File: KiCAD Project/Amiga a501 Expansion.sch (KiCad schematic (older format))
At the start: 4 parts, among them J1 Conn_02x28_Odd_Even, U1 AS7C4098A, U2 AS7C4098A

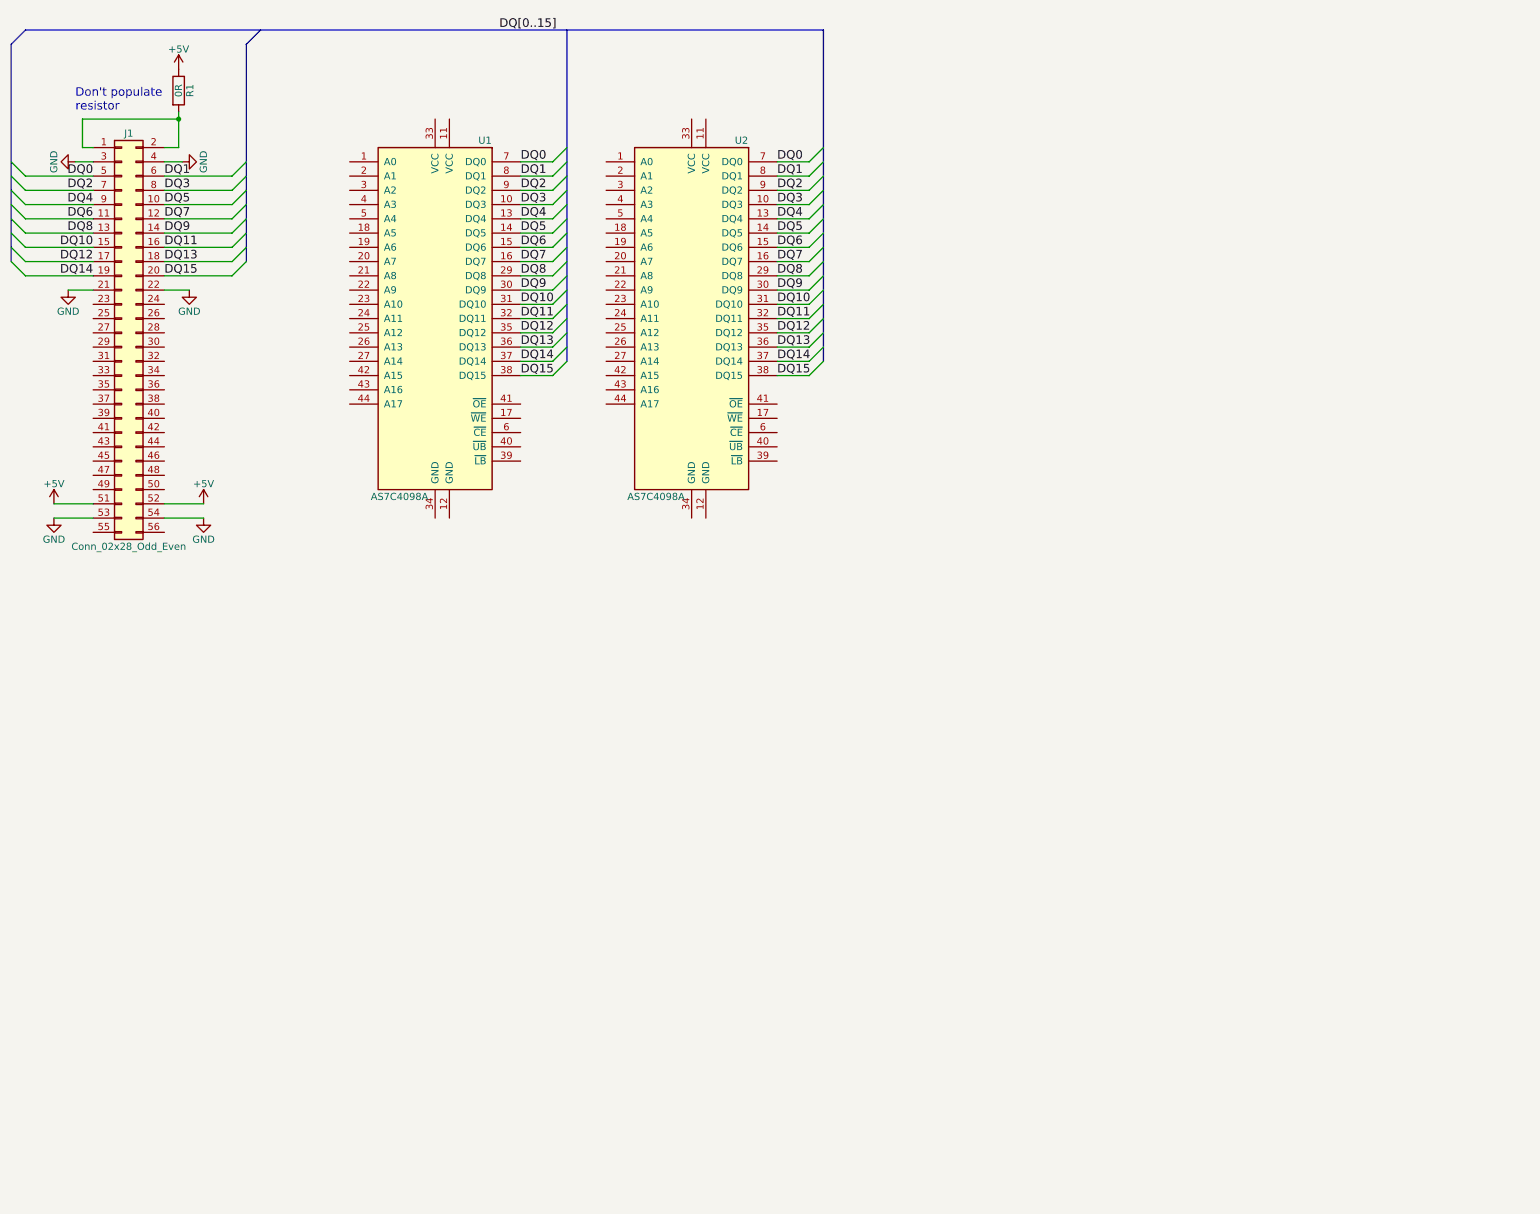
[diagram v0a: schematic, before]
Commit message: Work on verilog files. Started ram controller, made a flip flop array. Learning verilator synthesis now
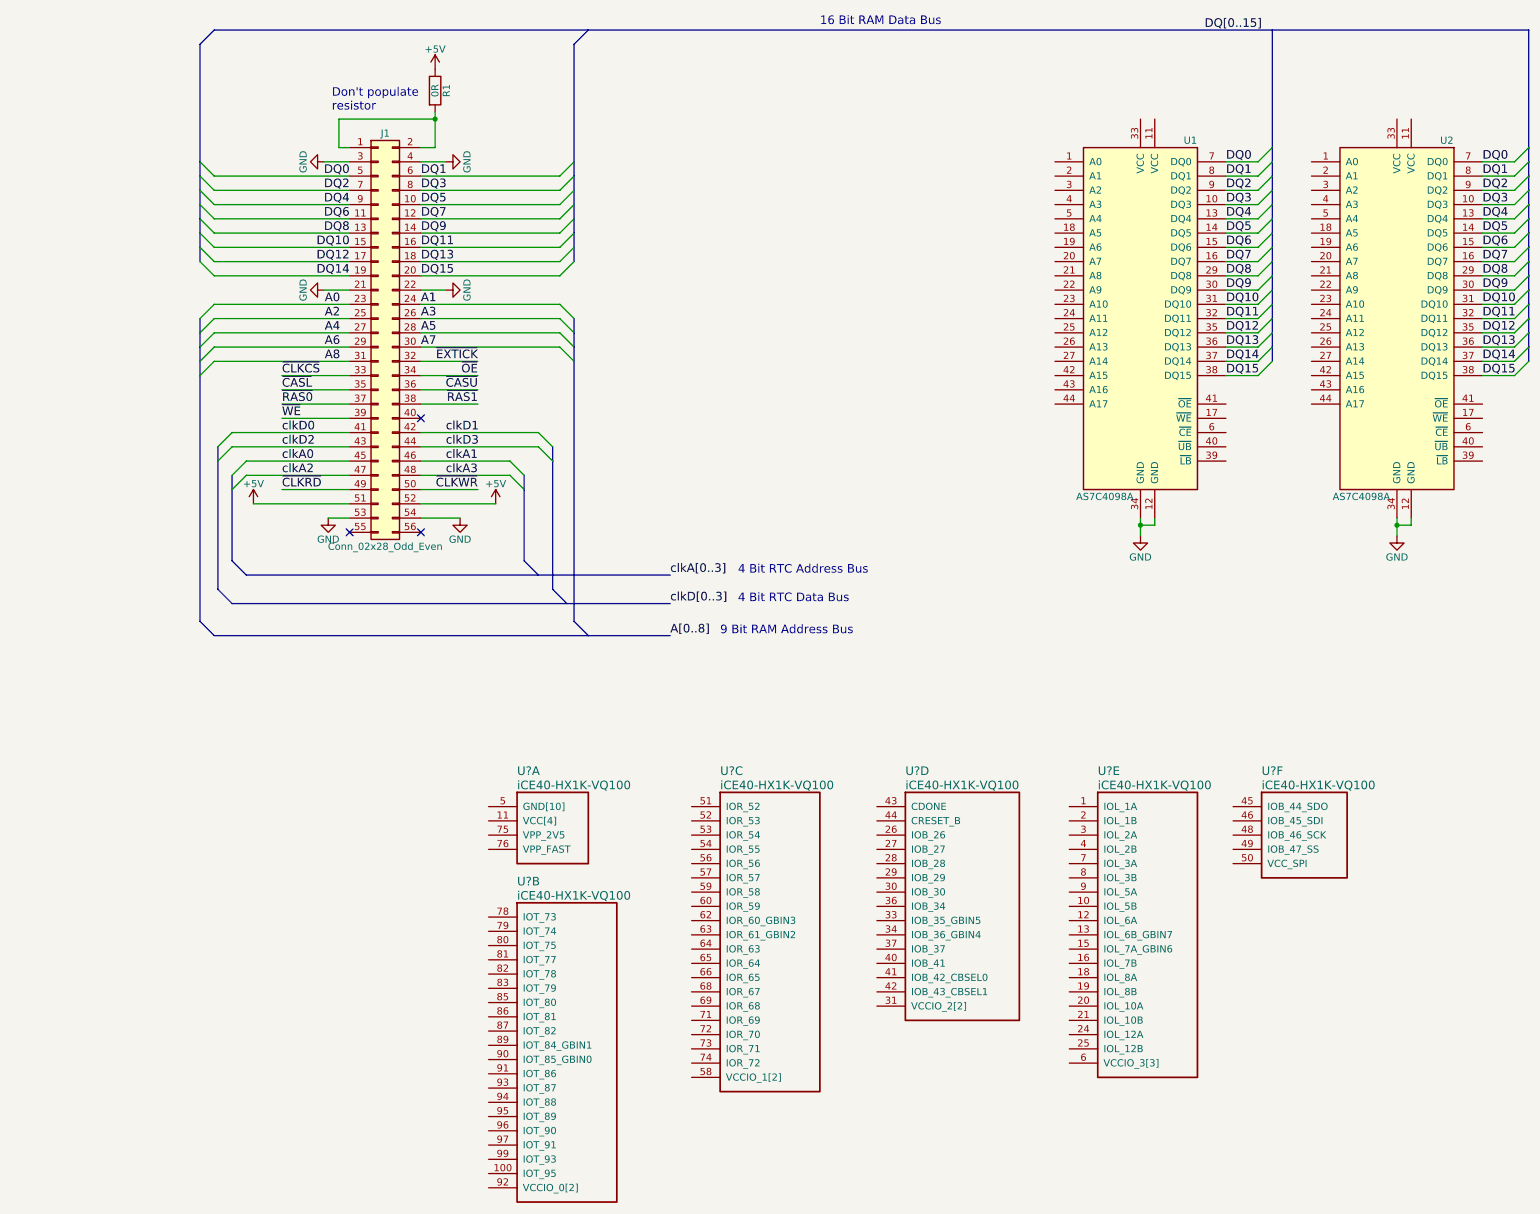
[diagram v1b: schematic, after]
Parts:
- added U? (x6): iCE40-HX1K-VQ100, symbol iCE40-HX1K-VQ100
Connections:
- net GND: now also U1.12 (GND), U1.34 (GND), U2.12 (GND), U2.34 (GND)
- net A0: now reaches J1.23 (Pin_23)
- net A1: now reaches J1.24 (Pin_24)
- net A2: now reaches J1.25 (Pin_25)
- net A3: now reaches J1.26 (Pin_26)
- net A4: now reaches J1.27 (Pin_27)
- net A5: now reaches J1.28 (Pin_28)
- net A6: now reaches J1.29 (Pin_29)
- net A7: now reaches J1.30 (Pin_30)
- net A8: now reaches J1.31 (Pin_31)
- net ~EXTICK: now reaches J1.32 (Pin_32)
- net ~CLKCS: now reaches J1.33 (Pin_33)
- net ~OE: now reaches J1.34 (Pin_34)
- net ~CASL: now reaches J1.35 (Pin_35)
- net ~CASU: now reaches J1.36 (Pin_36)
- net ~RAS0: now reaches J1.37 (Pin_37)
- net ~RAS1: now reaches J1.38 (Pin_38)
- net ~WE: now reaches J1.39 (Pin_39)
- net clkD0: now reaches J1.41 (Pin_41)
- net clkD1: now reaches J1.42 (Pin_42)
- net clkD2: now reaches J1.43 (Pin_43)
- net clkD3: now reaches J1.44 (Pin_44)
- net clkA0: now reaches J1.45 (Pin_45)
- net clkA1: now reaches J1.46 (Pin_46)
- net clkA2: now reaches J1.47 (Pin_47)
- net clkA3: now reaches J1.48 (Pin_48)
- net ~CLKRD: now reaches J1.49 (Pin_49)
- net ~CLKWR: now reaches J1.50 (Pin_50)
- new net: U?.11 (VCC[4]), U?.35 (VCC[4]), U?.61 (VCC[4]), U?.77 (VCC[4])
- new net: U?.17 (GND[10]), U?.23 (GND[10]), U?.32 (GND[10]), U?.39 (GND[10]), U?.47 (GND[10]), U?.5 (GND[10]), U?.55 (GND[10]), U?.70 (GND[10]), U?.84 (GND[10]), U?.98 (GND[10])
- new net: U?.88 (VCCIO_0[2]), U?.92 (VCCIO_0[2])
- new net: U?.58 (VCCIO_1[2]), U?.67 (VCCIO_1[2])
- new net: U?.31 (VCCIO_2[2]), U?.38 (VCCIO_2[2])
- new net: U?.14 (VCCIO_3[3]), U?.22 (VCCIO_3[3]), U?.6 (VCCIO_3[3])
- no-connect marks 0 -> 3
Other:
- note added: "16 Bit RAM Data Bus"
- note added: "4 Bit RTC Address Bus"
- note added: "4 Bit RTC Data Bus"
- note added: "9 Bit RAM Address Bus"
- moved on the sheet: J1, R1, U1, U2
